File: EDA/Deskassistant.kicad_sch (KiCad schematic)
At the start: 10 parts, among them J1 Conn_01x04_Socket, SW1 SW_MEC_5G, SW2 SW_MEC_5G, SW3 SW_MEC_5G, SW4 SW_MEC_5G, U1 Mic, U2 ESP32-S3-DevKitC, U3 ESP32-C3-MINI-1, U4 Soil moisture thing, U5 Soil temp thing

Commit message: EDA
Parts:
- added R1: 4.7k, symbol Device:R
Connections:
- net at U5.3 (GND): now also U3.1 (GND), U3.11 (GND), U3.14 (GND), U3.2 (GND), U3.36 (GND), U3.37 (GND), U3.38 (GND), U3.39 (GND), U3.40 (GND), U3.41 (GND), U3.42 (GND), U3.43 (GND), U3.44 (GND), U3.45 (GND), U3.46 (GND), U3.47 (GND), U3.48 (GND), U3.49 (GND), U3.50 (GND), U3.51 (GND), U3.52 (GND), U3.53 (GND), U4.3 (GND)
- net at U3.13 (GPIO1/ADC1_CH1/XTAL_32K_N): now also U5.3 (GND), R1.1
- new net: R1.2, U3.3 (3V3), U4.3 (GND), U5.3 (GND)
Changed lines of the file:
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@@
   (junction (at 166.37 130.81) (diameter 0) (color 0 0 0 0)
   )
+  (junction (at 231.14 102.87) (diameter 0) (color 0 0 0 0)
+  )
   (junction (at 110.49 125.73) (diameter 0) (color 0 0 0 0)
   )
   (junction (at 113.03 125.73) (diameter 0) (color 0 0 0 0)
   )
+  (junction (at 215.9 101.6) (diameter 0) (color 0 0 0 0)
+  )
   (wire (pts (xy 160.02 80.01) (xy 160.02 90.17))
     (stroke (width 0) (type default))
@@
     (stroke (width 0) (type default))
   )
+  (wire (pts (xy 207.01 132.08) (xy 207.01 101.6))
+    (stroke (width 0) (type default))
+  )
   (wire (pts (xy 160.02 69.85) (xy 160.02 80.01))
     (stroke (width 0) (type default))
   )
+  (wire (pts (xy 231.14 96.52) (xy 231.14 102.87))
+    (stroke (width 0) (type default))
+  )
   (wire (pts (xy 36.83 128.27) (xy 36.83 33.02))
     (stroke (width 0) (type default))
@@
     (stroke (width 0) (type default))
   )
+  (wire (pts (xy 207.01 101.6) (xy 215.9 101.6))
+    (stroke (width 0) (type default))
+  )
   (wire (pts (xy 119.38 15.24) (xy 64.77 15.24))
     (stroke (width 0) (type default))
   )
-  (wire (pts (xy 215.9 102.87) (xy 215.9 85.09))
+  (wire (pts (xy 215.9 102.87) (xy 215.9 101.6))
     (stroke (width 0) (type default))
   )
@@
     (stroke (width 0) (type default))
   )
+  (wire (pts (xy 179.07 96.52) (xy 231.14 96.52))
+    (stroke (width 0) (type default))
+  )
   (wire (pts (xy 149.86 90.17) (xy 149.86 137.16))
     (stroke (width 0) (type default))
@@
     (stroke (width 0) (type default))
   )
+  (wire (pts (xy 231.14 102.87) (xy 236.22 102.87))
+    (stroke (width 0) (type default))
+  )
   (wire (pts (xy 149.86 76.2) (xy 149.86 80.01))
     (stroke (width 0) (type default))
   )
+  (wire (pts (xy 204.47 35.56) (xy 179.07 35.56))
+    (stroke (width 0) (type default))
+  )
   (wire (pts (xy 100.33 78.74) (xy 91.44 78.74))
     (stroke (width 0) (type default))
   )
+  (wire (pts (xy 236.22 124.46) (xy 228.6 124.46))
+    (stroke (width 0) (type default))
+  )
   (wire (pts (xy 125.73 40.64) (xy 110.49 40.64))
     (stroke (width 0) (type default))
   )
+  (wire (pts (xy 236.22 102.87) (xy 236.22 124.46))
+    (stroke (width 0) (type default))
+  )
   (wire (pts (xy 64.77 15.24) (xy 64.77 20.32))
     (stroke (width 0) (type default))
@@
     (stroke (width 0) (type default))
   )
+  (wire (pts (xy 179.07 35.56) (xy 179.07 96.52))
+    (stroke (width 0) (type default))
+  )
   (wire (pts (xy 198.12 100.33) (xy 167.64 100.33))
     (stroke (width 0) (type default))
   )
+  (wire (pts (xy 228.6 132.08) (xy 207.01 132.08))
+    (stroke (width 0) (type default))
+  )
   (wire (pts (xy 154.94 128.27) (xy 36.83 128.27))
     (stroke (width 0) (type default))
@@
     (stroke (width 0) (type default))
   )
+  (wire (pts (xy 215.9 101.6) (xy 215.9 85.09))
+    (stroke (width 0) (type default))
+  )
   (wire (pts (xy 215.9 85.09) (xy 201.93 85.09))
     (stroke (width 0) (type default))
@@
   )
   (wire (pts (xy 243.84 104.14) (xy 241.3 104.14))
+    (stroke (width 0) (type default))
+  )
+  (wire (pts (xy 223.52 102.87) (xy 231.14 102.87))
     (stroke (width 0) (type default))
   )
@@
         )
       )
+    )
+  )
+  (symbol (lib_id "Device:R") (at 228.6 128.27 0) (unit 1)
+    (in_bom yes) (on_board yes) (dnp no) (fields_autoplaced)
+    (property "Reference" "R1" (at 231.14 127 0)
+      (effects (font (size 1.27 1.27)) (justify left))
+    )
+    (property "Value" "4.7k" (at 231.14 129.54 0)
+      (effects (font (size 1.27 1.27)) (justify left))
+    )
+    (property "Footprint" "" (at 226.822 128.27 90)
+      (effects (font (size 1.27 1.27)) hide)
+    )
+    (property "Datasheet" "~" (at 228.6 128.27 0)
+      (effects (font (size 1.27 1.27)) hide)
+    )
+    (pin "1")
+    (pin "2")
+    (instances
+      (project "Deskassistant"
+        (path "/a3984d46-aa45-43ad-9d15-0b2e957d0aa2"
+          (reference "R1") (unit 1)
+        )
+      )

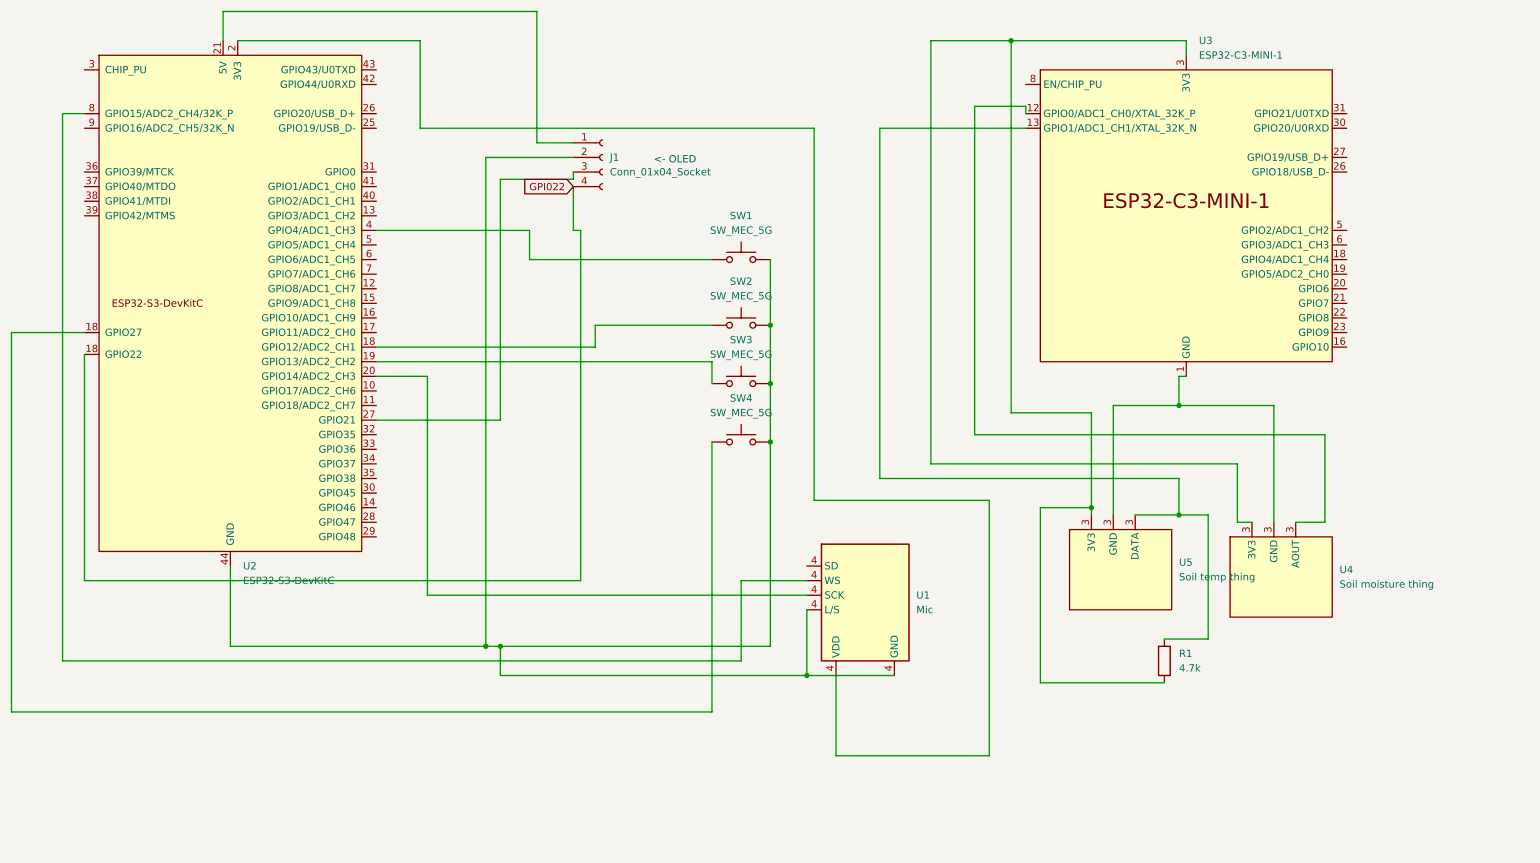
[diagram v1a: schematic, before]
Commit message: Added LiPo
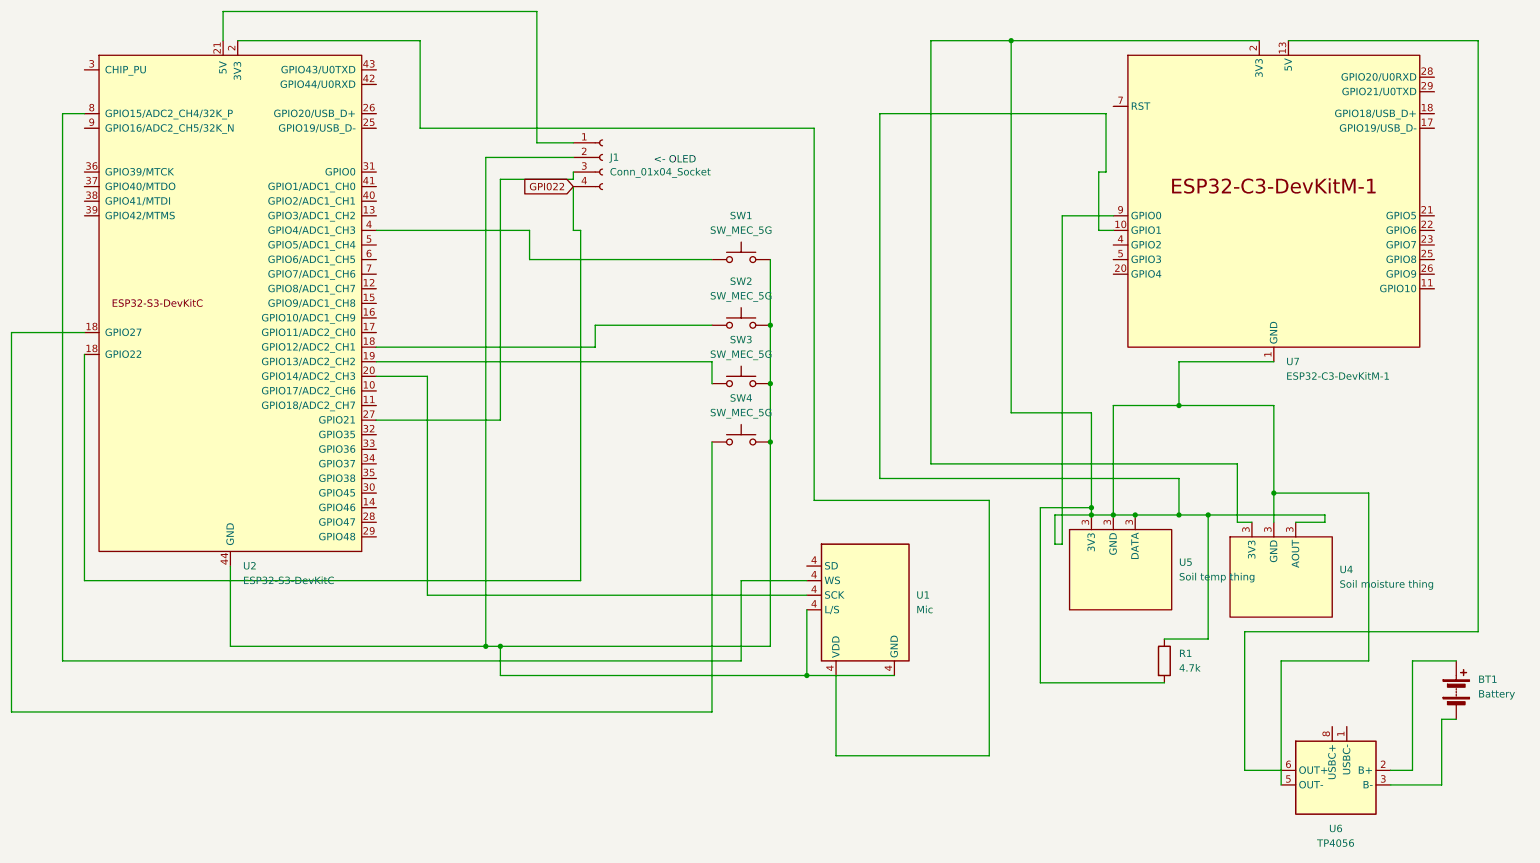
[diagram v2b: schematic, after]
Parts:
- removed U3: ESP32-C3-MINI-1, PCM_Espressif:ESP32-C3-MINI-1, symbol nn:ESP32-C3-MINI-1
- added BT1: Battery, symbol Device:Battery
- added U6: TP4056, symbol nn:47L04
- added U7: ESP32-C3-DevKitM-1, PCM_Espressif:ESP32-C3-DevKitM-1, symbol nn:ESP32-C3-DevKitM-1
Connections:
- net 3V3: now reaches R1.1, U5.3 (DATA)
- net 3V3: now also R1.2, U4.3 (AOUT), U6.5 (OUT-), U7.1 (GND), U7.10 (GPIO1), U7.12 (GND), U7.15 (GND), U7.16 (GND), U7.19 (GND), U7.2 (3V3), U7.24 (GND), U7.27 (GND), U7.3 (3V3), U7.30 (GND), U7.6 (GND), U7.8 (GND), U7.9 (GPIO0)
- new net: BT1.1 (+), U6.2 (B+)
- new net: BT1.2 (-), U6.3 (B-)
- new net 5V: U6.6 (OUT+), U7.13 (5V), U7.14 (5V)
